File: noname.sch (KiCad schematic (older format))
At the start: 25 parts, among them P1 CONN_01X07, U1 MSP430G2955IRHA40, U3 RT9193

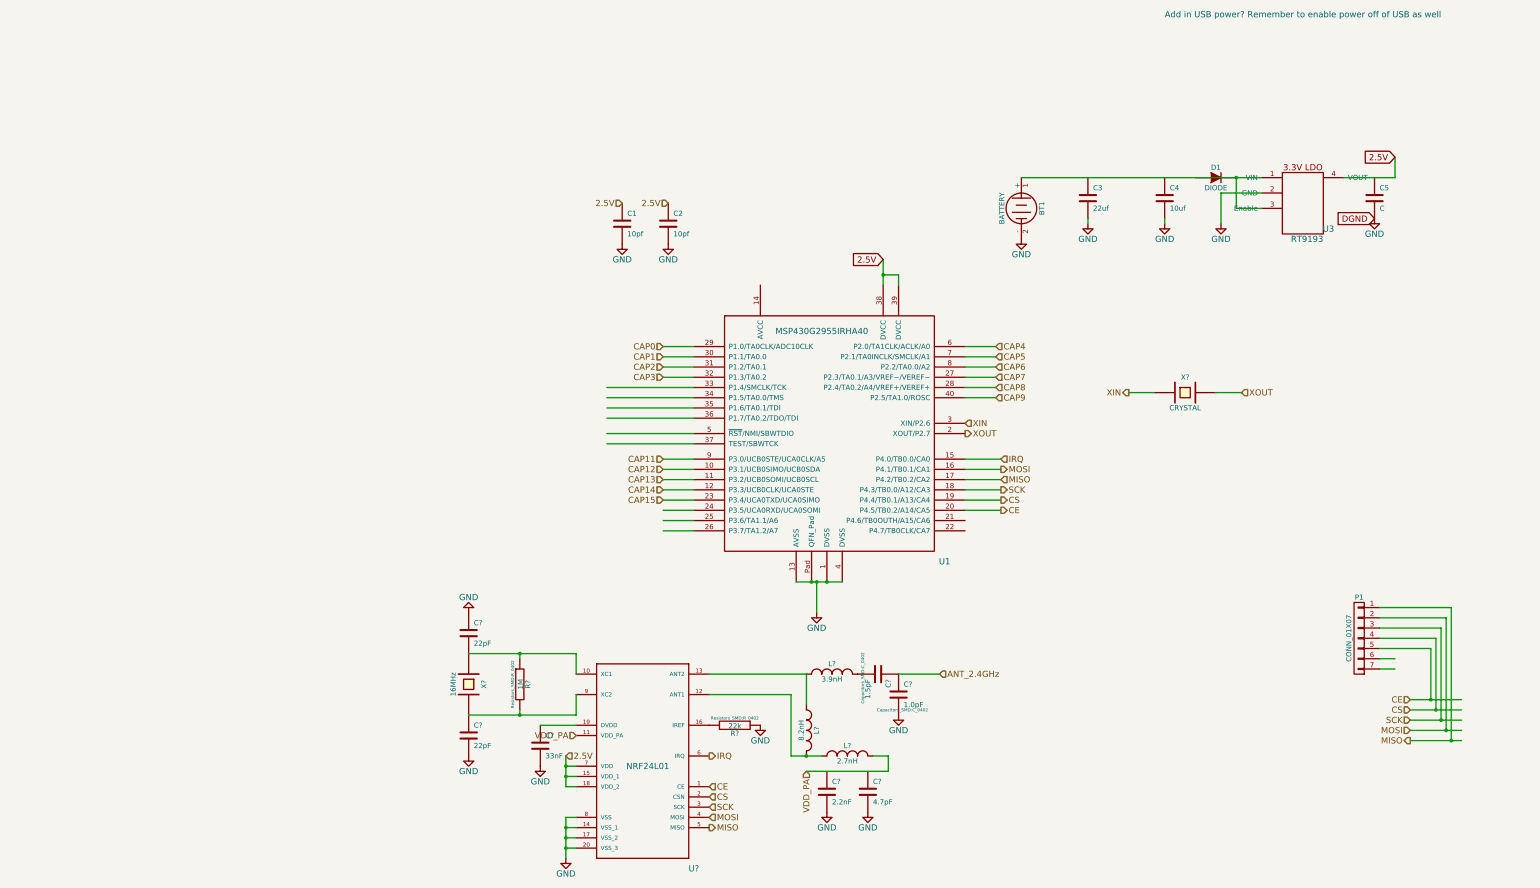
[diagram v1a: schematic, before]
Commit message: using new uC
MSP430G2553 TSSOP 20 pin, lots of changes
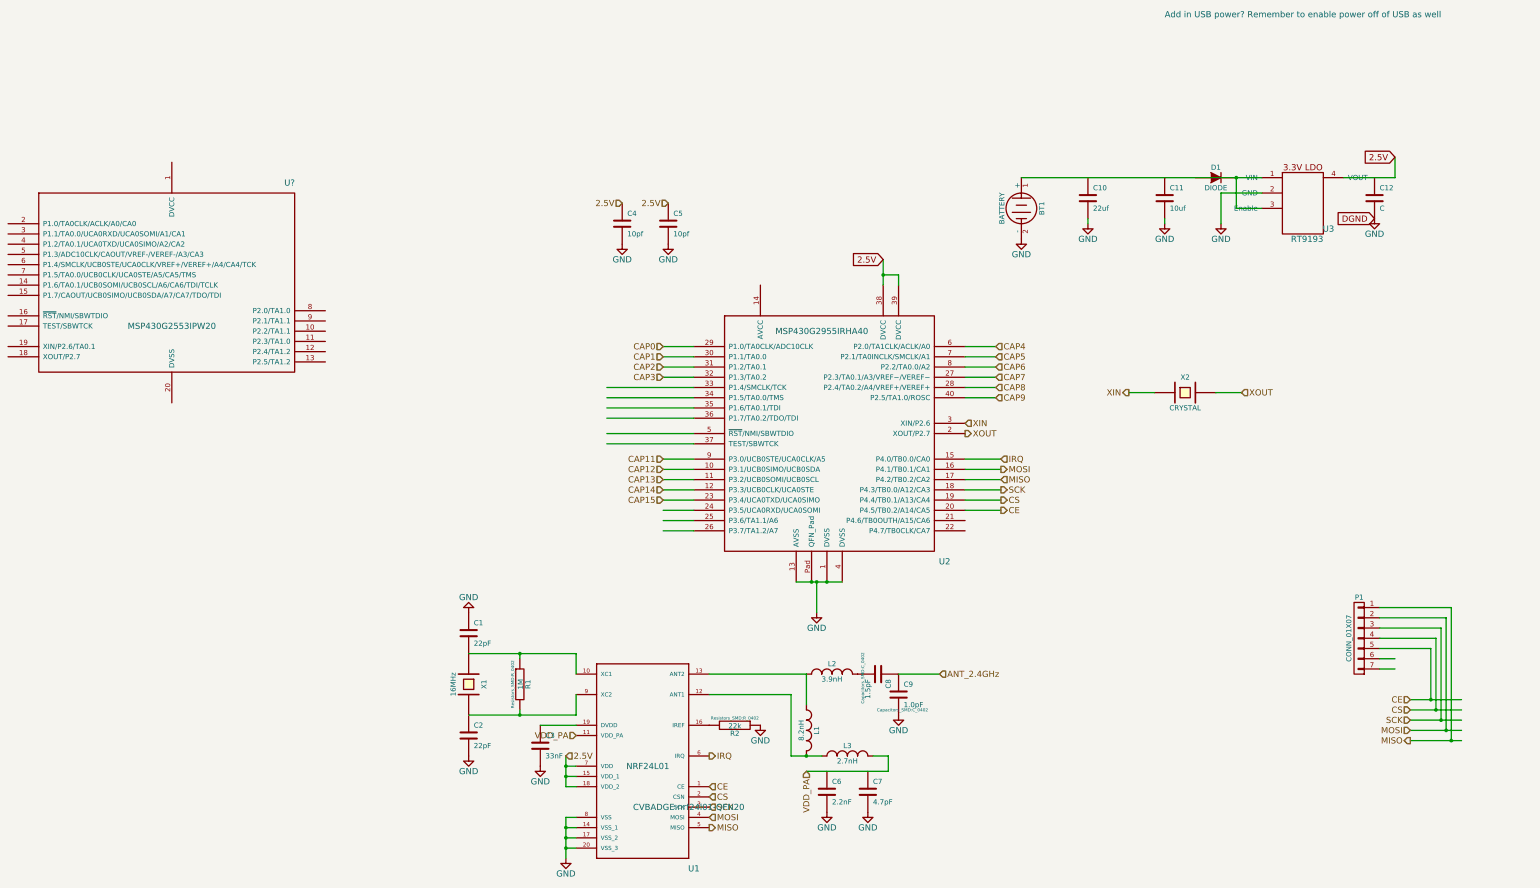
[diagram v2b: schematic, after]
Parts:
- added U?: MSP430G2553IPW20, symbol MSP430G2553IPW20
- C1, C2, C3: renamed from C?; footprint Capacitors_SMD:C_0402 -> (none)
- U1: renamed from U?; footprint (none) -> CVBADGE:nrf24l01-QFN20
- gave numbers to parts that had none: 11
- renumbered C3 to C10, C4 to C11, C5 to C12, C1 to C4, C2 to C5, U1 to U2
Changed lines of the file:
@@
 LIBS:nrf24l01
 LIBS:noname-cache
+LIBS:CV_BADGE
 EELAYER 25 0
 EELAYER END
@@
 $EndDescr
 $Comp
-L MSP430G2955IRHA40 U1
+L MSP430G2955IRHA40 U2
 U 1 1 54F240CC
 P 3600 2150
-F 0 "U1" H 5750 -250 60  0000 C CNN
+F 0 "U2" H 5750 -250 60  0000 C CNN
 F 1 "MSP430G2955IRHA40" H 4550 2000 60  0000 C CNN
-F 2 "" H 550 1650 60  0000 C CNN
+F 2 "" H 550 1650 60  0001 C CNN
 F 3 "" H 550 1650 60  0000 C CNN
 	1    3600 2150
@@
 F 0 "U3" H 9500 700 60  0000 C CNN
 F 1 "RT9193" H 9450 600 60  0000 R CNN
-F 2 "" H 9450 600 60  0000 C CNN
+F 2 "" H 9450 600 60  0001 C CNN
 F 3 "" H 9450 600 60  0000 C CNN
 	1    9250 1000
@@
 F 0 "BT1" H 6500 1300 50  0000 C CNN
 F 1 "BATTERY" H 6500 910 50  0000 C CNN
-F 2 "" H 6500 1100 60  0000 C CNN
+F 2 "" H 6500 1100 60  0001 C CNN
 F 3 "" H 6500 1100 60  0000 C CNN
 	1    6500 1100
@@
 $EndComp
 $Comp
-L C C3
+L C C10
 U 1 1 54F2528A
 P 7150 1000
-F 0 "C3" H 7200 1100 50  0000 L CNN
+F 0 "C10" H 7200 1100 50  0000 L CNN
 F 1 "22uf" H 7200 900 50  0000 L CNN
-F 2 "" H 7188 850 30  0000 C CNN
+F 2 "" H 7188 850 30  0001 C CNN
 F 3 "" H 7150 1000 60  0000 C CNN
 	1    7150 1000
@@
 $EndComp
 $Comp
-L C C4
+L C C11
 U 1 1 54F25371
 P 7900 1000
-F 0 "C4" H 7950 1100 50  0000 L CNN
+F 0 "C11" H 7950 1100 50  0000 L CNN
 F 1 "10uf" H 7950 900 50  0000 L CNN
-F 2 "" H 7938 850 30  0000 C CNN
+F 2 "" H 7938 850 30  0001 C CNN
 F 3 "" H 7900 1000 60  0000 C CNN
 	1    7900 1000
@@
 F 0 "D1" H 8400 900 50  0000 C CNN
 F 1 "DIODE" H 8400 700 50  0000 C CNN
-F 2 "" H 8400 800 60  0000 C CNN
+F 2 "" H 8400 800 60  0001 C CNN
 F 3 "" H 8400 800 60  0000 C CNN
 	1    8400 800
@@
 $EndComp
 $Comp
-L C C5
+L C C12
 U 1 1 54F256AA
 P 9950 1000
-F 0 "C5" H 10000 1100 50  0000 L CNN
+F 0 "C12" H 10000 1100 50  0000 L CNN
 F 1 "C" H 10000 900 50  0000 L CNN
-F 2 "" H 9988 850 30  0000 C CNN
+F 2 "" H 9988 850 30  0001 C CNN
 F 3 "" H 9950 1000 60  0000 C CNN
 	1    9950 1000
@@
 F 0 "P1" H 9800 5700 50  0000 C CNN
 F 1 "CONN_01X07" V 9900 5300 50  0000 C CNN
-F 2 "" H 9800 5300 60  0000 C CNN
+F 2 "" H 9800 5300 60  0001 C CNN
 F 3 "" H 9800 5300 60  0000 C CNN
 	1    9800 5300
@@
 CAP15
 $Comp
-L C C1
+L C C4
 U 1 1 54F2AA40
 P 2600 1250
-F 0 "C1" H 2650 1350 50  0000 L CNN
+F 0 "C4" H 2650 1350 50  0000 L CNN
 F 1 "10pf" H 2650 1150 50  0000 L CNN
-F 2 "" H 2638 1100 30  0000 C CNN
+F 2 "" H 2638 1100 30  0001 C CNN
 F 3 "" H 2600 1250 60  0000 C CNN
 	1    2600 1250
@@
 $EndComp
 $Comp
-L C C2
+L C C5
 U 1 1 54F2AC61
 P 3050 1250
-F 0 "C2" H 3100 1350 50  0000 L CNN
+F 0 "C5" H 3100 1350 50  0000 L CNN
 F 1 "10pf" H 3100 1150 50  0000 L CNN
-F 2 "" H 3088 1100 30  0000 C CNN
+F 2 "" H 3088 1100 30  0001 C CNN
 F 3 "" H 3050 1250 60  0000 C CNN
 	1    3050 1250
@@
 2.5V
 $Comp
-L NRF24L01 U?
+L NRF24L01 U1
 U 1 1 54F3687D
 P 2850 6550
-F 0 "U?" H 3300 5550 60  0000 C CNN
+F 0 "U1" H 3300 5550 60  0000 C CNN
 F 1 "NRF24L01" H 2850 6550 60  0000 C CNN
-F 2 "" H 3250 6150 60  0000 C CNN
+F 2 "CVBADGE:nrf24l01-QFN20" H 3250 6150 60  0000 C CNN
 F 3 "" H 3250 6150 60  0000 C CNN
 	1    2850 6550
@@
 IRQ
 $Comp
-L GND #PWR?
+L GND #PWR09
 U 1 1 54F382B4
 P 2050 7450
-F 0 "#PWR?" H 2050 7200 60  0001 C CNN
+F 0 "#PWR09" H 2050 7200 60  0001 C CNN
 F 1 "GND" H 2050 7300 60  0000 C CNN
 F 2 "" H 2050 7450 60  0000 C CNN
@@
 	2150 6150 1800 6150
 $Comp
-L C C?
+L C C3
 U 1 1 54F38994
 P 1800 6350
-F 0 "C?" H 1850 6450 50  0000 L CNN
+F 0 "C3" H 1850 6450 50  0000 L CNN
 F 1 "33nF" H 1850 6250 50  0000 L CNN
-F 2 "Capacitors_SMD:C_0402" H 1838 6200 30  0001 C CNN
+F 2 "" H 1838 6200 30  0001 C CNN
 F 3 "" H 1800 6350 60  0000 C CNN
 	1    1800 6350
@@
 $EndComp
 $Comp
-L GND #PWR?
+L GND #PWR010
 U 1 1 54F38A03
 P 1800 6550
-F 0 "#PWR?" H 1800 6300 60  0001 C CNN
+F 0 "#PWR010" H 1800 6300 60  0001 C CNN
 F 1 "GND" H 1800 6400 60  0000 C CNN
 F 2 "" H 1800 6550 60  0000 C CNN
@@
 $EndComp
 $Comp
-L CRYSTAL X?
+L CRYSTAL X1
 U 1 1 54F38B90
 P 1100 5750
-F 0 "X?" H 1100 5900 50  0000 C CNN
+F 0 "X1" H 1100 5900 50  0000 C CNN
 F 1 "16MHz" H 1100 5600 50  0000 C CNN
-F 2 "" H 1100 5750 60  0000 C CNN
+F 2 "" H 1100 5750 60  0001 C CNN
 F 3 "" H 1100 5750 60  0000 C CNN
 	1    1100 5750
@@
 	2150 6050 1100 6050
 $Comp
-L C C?
+L C C1
 U 1 1 54F38F1D
 P 1100 5250
-F 0 "C?" H 1150 5350 50  0000 L CNN
+F 0 "C1" H 1150 5350 50  0000 L CNN
 F 1 "22pF" H 1150 5150 50  0000 L CNN
-F 2 "Capacitors_SMD:C_0402" H 1138 5100 30  0001 C CNN
+F 2 "" H 1138 5100 30  0001 C CNN
 F 3 "" H 1100 5250 60  0000 C CNN
 	1    1100 5250
@@
 $EndComp
 $Comp
-L C C?
+L C C2
 U 1 1 54F38F7C
 P 1100 6250
-F 0 "C?" H 1150 6350 50  0000 L CNN
+F 0 "C2" H 1150 6350 50  0000 L CNN
 F 1 "22pF" H 1150 6150 50  0000 L CNN
-F 2 "Capacitors_SMD:C_0402" H 1138 6100 30  0001 C CNN
+F 2 "" H 1138 6100 30  0001 C CNN
 F 3 "" H 1100 6250 60  0000 C CNN
 	1    1100 6250
@@
 $EndComp
 $Comp
-L GND #PWR?
+L GND #PWR011
 U 1 1 54F39042
 P 1100 6450
-F 0 "#PWR?" H 1100 6200 60  0001 C CNN
+F 0 "#PWR011" H 1100 6200 60  0001 C CNN
 F 1 "GND" H 1100 6300 60  0000 C CNN
 F 2 "" H 1100 6450 60  0000 C CNN
@@
 $EndComp
 $Comp
-L GND #PWR?
+L GND #PWR012
 U 1 1 54F39056
 P 1100 5050
-F 0 "#PWR?" H 1100 4800 60  0001 C CNN
+F 0 "#PWR012" H 1100 4800 60  0001 C CNN
 F 1 "GND" H 1100 4900 60  0000 C CNN
 F 2 "" H 1100 5050 60  0000 C CNN
@@
 $EndComp
 $Comp
-L INDUCTOR_SMALL L?
+L INDUCTOR_SMALL L2
 U 1 1 54F3949A
 P 4650 5650
-F 0 "L?" H 4650 5750 50  0000 C CNN
+F 0 "L2" H 4650 5750 50  0000 C CNN
 F 1 "3.9nH" H 4650 5600 50  0000 C CNN
 F 2 "Capacitors_SMD:C_0402" H 4650 5650 60  0001 C CNN
@@
 $EndComp
 $Comp
-L INDUCTOR_SMALL L?
+L INDUCTOR_SMALL L1
 U 1 1 54F39523
 P 4400 6200
-F 0 "L?" H 4400 6300 50  0000 C CNN
+F 0 "L1" H 4400 6300 50  0000 C CNN
 F 1 "8.2nH" H 4400 6150 50  0000 C CNN
 F 2 "Capacitors_SMD:C_0402" H 4400 6200 60  0001 C CNN
@@
 $EndComp
 $Comp
-L INDUCTOR_SMALL L?
+L INDUCTOR_SMALL L3
 U 1 1 54F39568
 P 4800 6450
-F 0 "L?" H 4800 6550 50  0000 C CNN
+F 0 "L3" H 4800 6550 50  0000 C CNN
 F 1 "2.7nH" H 4800 6400 50  0000 C CNN
 F 2 "Capacitors_SMD:C_0402" H 4800 6450 60  0001 C CNN
@@
 VDD_PA
 $Comp
-L C C?
+L C C6
 U 1 1 54F39834
 P 4600 6800
-F 0 "C?" H 4650 6900 50  0000 L CNN
+F 0 "C6" H 4650 6900 50  0000 L CNN
 F 1 "2.2nF" H 4650 6700 50  0000 L CNN
 F 2 "Capacitors_SMD:C_0402" H 4638 6650 30  0001 C CNN
@@
 $EndComp
 $Comp
-L C C?
+L C C7
 U 1 1 54F39891
 P 5000 6800
-F 0 "C?" H 5050 6900 50  0000 L CNN
+F 0 "C7" H 5050 6900 50  0000 L CNN
 F 1 "4.7pF" H 5050 6700 50  0000 L CNN
 F 2 "Capacitors_SMD:C_0402" H 5038 6650 30  0001 C CNN
@@
 $EndComp
 $Comp
-L GND #PWR?
+L GND #PWR013
 U 1 1 54F398E8
 P 4600 7000
-F 0 "#PWR?" H 4600 6750 60  0001 C CNN
+F 0 "#PWR013" H 4600 6750 60  0001 C CNN
 F 1 "GND" H 4600 6850 60  0000 C CNN
 F 2 "" H 4600 7000 60  0000 C CNN
@@
 $EndComp
 $Comp
-L GND #PWR?
+L GND #PWR014
 U 1 1 54F398FC
 P 5000 7000
-F 0 "#PWR?" H 5000 6750 60  0001 C CNN
+F 0 "#PWR014" H 5000 6750 60  0001 C CNN
 F 1 "GND" H 5000 6850 60  0000 C CNN
 F 2 "" H 5000 7000 60  0000 C CNN
@@
 $EndComp
 $Comp
-L C C?
+L C C8
 U 1 1 54F39A63
 P 5100 5650
-F 0 "C?" H 5150 5750 50  0000 L CNN
+F 0 "C8" H 5150 5750 50  0000 L CNN
 F 1 "1.5pF" H 5150 5550 50  0000 L CNN
 F 2 "Capacitors_SMD:C_0402" H 5138 5500 30  0000 C CNN
@@
 $EndComp
 $Comp
-L C C?
+L C C9
 U 1 1 54F39AA6
 P 5300 5850
-F 0 "C?" H 5350 5950 50  0000 L CNN
+F 0 "C9" H 5350 5950 50  0000 L CNN
 F 1 "1.0pF" H 5350 5750 50  0000 L CNN
 F 2 "Capacitors_SMD:C_0402" H 5338 5700 30  0000 C CNN
@@
 Connection ~ 4400 6450
 $Comp
-L R R?
+L R R2
 U 1 1 54F3A73F
 P 3700 6150
-F 0 "R?" V 3780 6150 50  0000 C CNN
+F 0 "R2" V 3780 6150 50  0000 C CNN
 F 1 "22k" V 3707 6151 50  0000 C CNN
 F 2 "Resistors_SMD:R_0402" V 3630 6150 30  0000 C CNN
@@
 $EndComp
 $Comp
-L GND #PWR?
+L GND #PWR015
 U 1 1 54F3A7BE
 P 3950 6150
-F 0 "#PWR?" H 3950 5900 60  0001 C CNN
+F 0 "#PWR015" H 3950 5900 60  0001 C CNN
 F 1 "GND" H 3950 6000 60  0000 C CNN
 F 2 "" H 3950 6150 60  0000 C CNN
@@
 	7800 2900 7550 2900
 $Comp
-L CRYSTAL X?
+L CRYSTAL X2
 U 1 1 54F3BBDA
 P 8100 2900
-F 0 "X?" H 8100 3050 50  0000 C CNN
+F 0 "X2" H 8100 3050 50  0000 C CNN
 F 1 "CRYSTAL" H 8100 2750 50  0000 C CNN
-F 2 "" H 8100 2900 60  0000 C CNN
+F 2 "" H 8100 2900 60  0001 C CNN
 F 3 "" H 8100 2900 60  0000 C CNN
 	1    8100 2900
@@
 XOUT
 $Comp
-L R R?
+L R R1
 U 1 1 54F3D0B5
 P 1600 5750
-F 0 "R?" V 1680 5750 50  0000 C CNN
+F 0 "R1" V 1680 5750 50  0000 C CNN
 F 1 "1M" V 1607 5751 50  0000 C CNN
 F 2 "Resistors_SMD:R_0402" V 1530 5750 30  0000 C CNN
@@
 Connection ~ 1600 6050
 $Comp
-L GND #PWR?
+L GND #PWR016
 U 1 1 54F3D939
 P 5300 6050
-F 0 "#PWR?" H 5300 5800 60  0001 C CNN
+F 0 "#PWR016" H 5300 5800 60  0001 C CNN
 F 1 "GND" H 5300 5900 60  0000 C CNN
 F 2 "" H 5300 6050 60  0000 C CNN
@@
 	1    0    0    -1
 $EndComp
+$Comp
+L MSP430G2553IPW20 U?
+U 1 1 54F53C54
+P -3100 950
+F 0 "U?" H -650 1050 60  0000 C CNN
+F 1 "MSP430G2553IPW20" H -1800 -350 60  0000 C CNN
+F 2 "" H -3100 950 60  0000 C CNN
+F 3 "" H -3100 950 60  0000 C CNN
+	1    -3100 950
+	1    0    0    -1
+$EndComp
